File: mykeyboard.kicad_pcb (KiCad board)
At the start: 2 copper layers, 91.4 x 55.9 mm, 29 parts, among them J1 MJ-4PP-9, J2 LED, SW1 SW_PUSH, SW2 SW_PUSH, SW3 SW_PUSH, SW4 SW_PUSH, SW5 SW_PUSH, SW6 SW_PUSH, SW7 SW_PUSH, SW8 SW_PUSH, SW9 SW_PUSH, U1 ProMicro

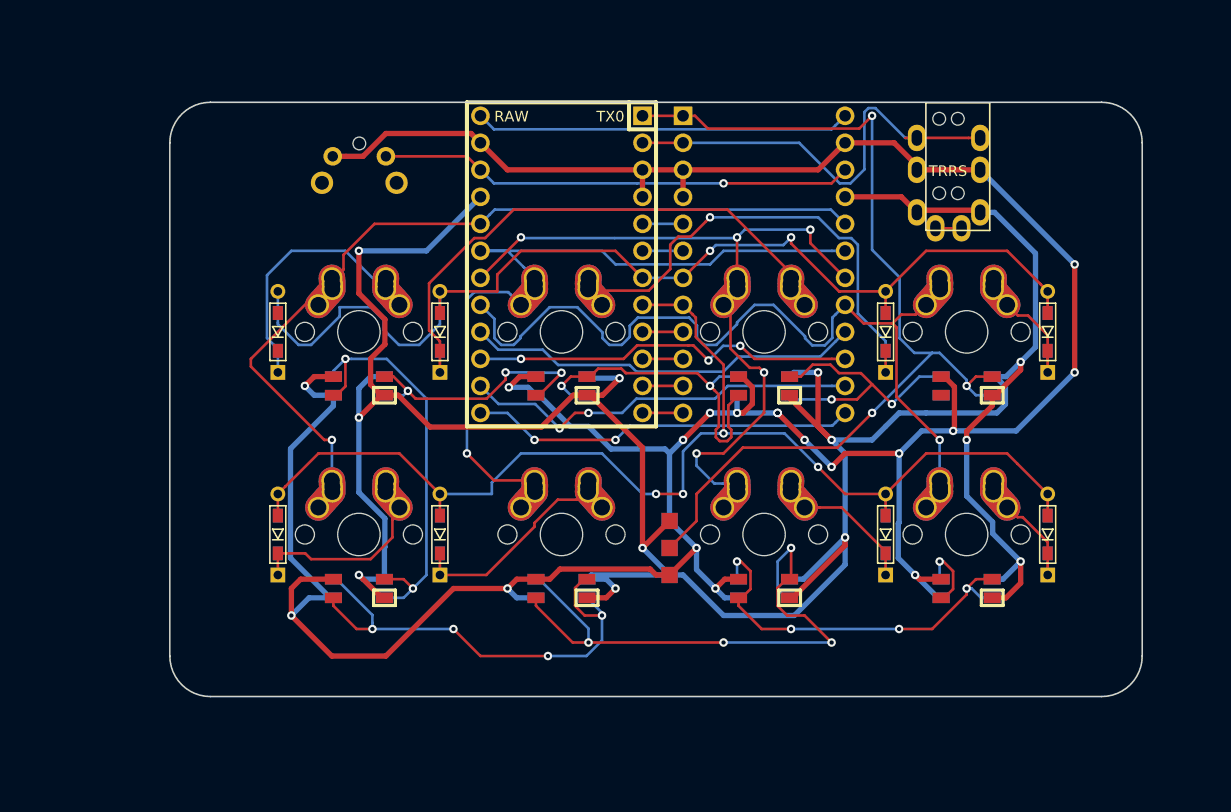
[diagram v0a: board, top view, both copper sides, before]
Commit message: スペーサの穴を確保
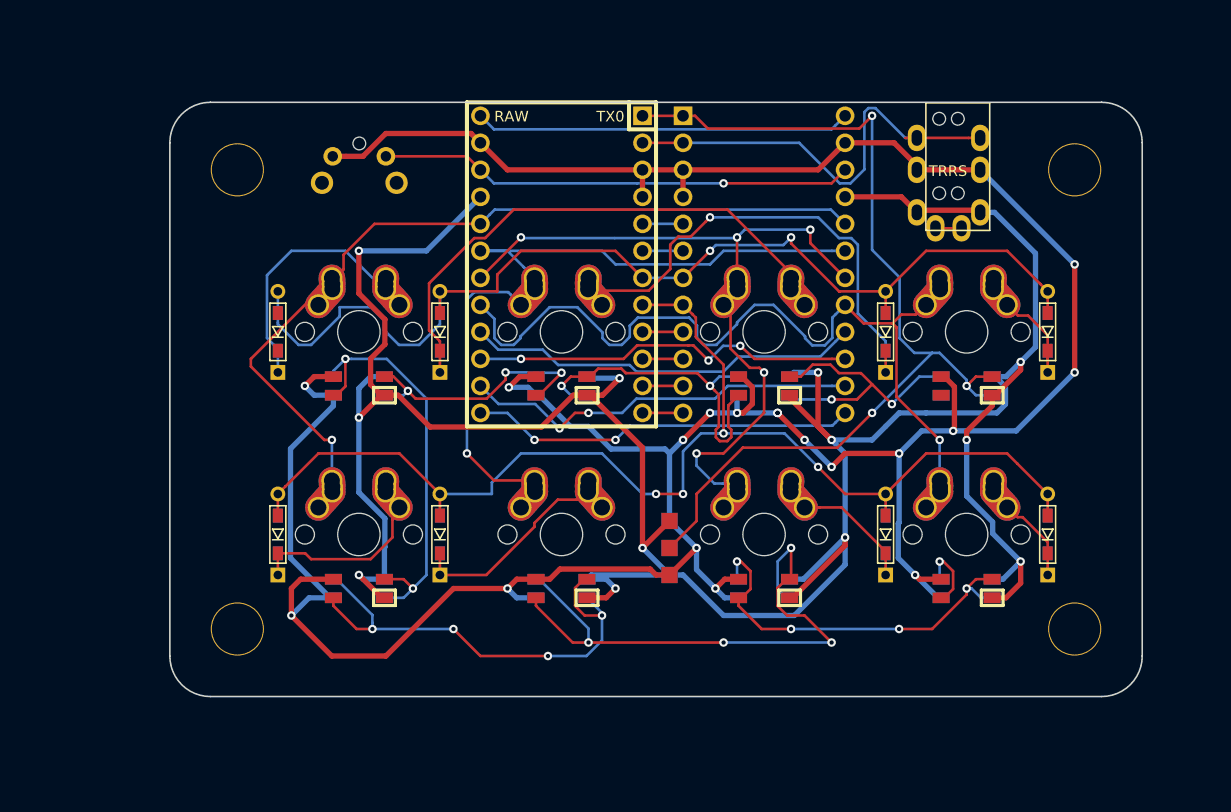
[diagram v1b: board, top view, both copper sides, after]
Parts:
- added Ref**: Val**, kbd:HOLE, F.Cu at (185.4, 81.3)
- added Ref**: Val**, kbd:HOLE, F.Cu at (185.4, 124.5)
- added Ref**: Val**, kbd:HOLE, F.Cu at (106.7, 124.5)
- added Ref**: Val**, kbd:HOLE, F.Cu at (106.7, 81.3)
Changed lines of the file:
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@@
     (tracks 725)
     (zones 0)
-    (modules 29)
+    (modules 33)
     (nets 40)
   )
@@
     (add_net row1)
   )
+  (module kbd:HOLE (layer F.Cu)
+    (at 185.42 81.28)
+    (descr "Mounting Hole 2.2mm, no annular, M2")
+    (tags "mounting hole 2.2mm no annular m2")
+    (attr virtual)
+    (fp_text reference Ref** (at 0 -3.2) (layer F.Fab)
+      (effects (font (size 1 1) (thickness 0.15)))
+    )
+    (fp_text value Val** (at 0 3.2) (layer F.Fab)
+      (effects (font (size 1 1) (thickness 0.15)))
+    )
+    (fp_text user %R (at 0.3 0) (layer F.Fab)
+      (effects (font (size 1 1) (thickness 0.15)))
+    )
+    (fp_circle (center 0 0) (end 2.2 0) (layer Cmts.User) (width 0.15))
+    (fp_circle (center 0 0) (end 2.45 0) (layer F.CrtYd) (width 0.05))
+    (pad "" np_thru_hole circle (at 0 0) (size 5 5) (drill 4.8) (layers *.Cu *.Mask))
+  )
+  (module kbd:HOLE (layer F.Cu)
+    (at 185.42 124.46)
+    (descr "Mounting Hole 2.2mm, no annular, M2")
+    (tags "mounting hole 2.2mm no annular m2")
+    (attr virtual)
+    (fp_text reference Ref** (at 0 -3.2) (layer F.Fab)
+      (effects (font (size 1 1) (thickness 0.15)))
+    )
+    (fp_text value Val** (at 0 3.2) (layer F.Fab)
+      (effects (font (size 1 1) (thickness 0.15)))
+    )
+    (fp_circle (center 0 0) (end 2.45 0) (layer F.CrtYd) (width 0.05))
+    (fp_circle (center 0 0) (end 2.2 0) (layer Cmts.User) (width 0.15))
+    (fp_text user %R (at 0.3 0) (layer F.Fab)
+      (effects (font (size 1 1) (thickness 0.15)))
+    )
+    (pad "" np_thru_hole circle (at 0 0) (size 5 5) (drill 4.8) (layers *.Cu *.Mask))
+  )
+  (module kbd:HOLE (layer F.Cu)
+    (at 106.68 124.46)
+    (descr "Mounting Hole 2.2mm, no annular, M2")
+    (tags "mounting hole 2.2mm no annular m2")
+    (attr virtual)
+    (fp_text reference Ref** (at 0 -3.2) (layer F.Fab)
+      (effects (font (size 1 1) (thickness 0.15)))
+    )
+    (fp_text value Val** (at 0 3.2) (layer F.Fab)
+      (effects (font (size 1 1) (thickness 0.15)))
+    )
+    (fp_text user %R (at 0.3 0) (layer F.Fab)
+      (effects (font (size 1 1) (thickness 0.15)))
+    )
+    (fp_circle (center 0 0) (end 2.2 0) (layer Cmts.User) (width 0.15))
+    (fp_circle (center 0 0) (end 2.45 0) (layer F.CrtYd) (width 0.05))
+    (pad "" np_thru_hole circle (at 0 0) (size 5 5) (drill 4.8) (layers *.Cu *.Mask))
+  )
+  (module kbd:HOLE (layer F.Cu)
+    (at 106.68 81.28)
+    (descr "Mounting Hole 2.2mm, no annular, M2")
+    (tags "mounting hole 2.2mm no annular m2")
+    (attr virtual)
+    (fp_text reference Ref** (at 0 -3.2) (layer F.Fab)
+      (effects (font (size 1 1) (thickness 0.15)))
+    )
+    (fp_text value Val** (at 0 3.2) (layer F.Fab)
+      (effects (font (size 1 1) (thickness 0.15)))
+    )
+    (fp_circle (center 0 0) (end 2.45 0) (layer F.CrtYd) (width 0.05))
+    (fp_circle (center 0 0) (end 2.2 0) (layer Cmts.User) (width 0.15))
+    (fp_text user %R (at 0.3 0) (layer F.Fab)
+      (effects (font (size 1 1) (thickness 0.15)))
+    )
+    (pad "" np_thru_hole circle (at 0 0) (size 5 5) (drill 4.8) (layers *.Cu *.Mask))
+  )
   (module Keebio-Parts:Hybrid_PCB_100H_Dual_hole (layer F.Cu)

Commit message: GND の塗りつぶし
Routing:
- added copper zone on B.Cu, net GND
- added copper zone on F.Cu, net GND
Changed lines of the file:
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@@
   (segment (start 172.72 119.635) (end 172.86 119.775) (width 0.25) (layer B.Cu) (net 39))
   (segment (start 172.72 118.11) (end 172.72 119.635) (width 0.25) (layer B.Cu) (net 39))
+  (zone (net 14) (net_name GND) (layer F.Cu) (hatch edge 0.508)
+    (connect_pads (clearance 0.508))
+    (min_thickness 0.254)
+    (fill yes (arc_segments 16) (thermal_gap 0.508) (thermal_bridge_width 0.508))
+    (polygon
+      (pts
+        (xy 194.31 133.35) (xy 194.31 73.66) (xy 99.06 72.39) (xy 96.52 130.81) (xy 99.06 135.89)
+      )
+    )
+  )
+  (zone (net 14) (net_name GND) (layer B.Cu) (hatch edge 0.508)
+    (connect_pads (clearance 0.508))
+    (min_thickness 0.254)
+    (fill yes (arc_segments 16) (thermal_gap 0.508) (thermal_bridge_width 0.508))
+    (polygon
+      (pts
+        (xy 196.85 134.62) (xy 198.12 72.39) (xy 86.36 67.31) (xy 90.17 139.7)
+      )
+    )
+  )
 )

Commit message: Add credit
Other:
- board text added: "wktk/id1kb v0.1 (2019-01-30) Designed by @wk wktk.jp/"
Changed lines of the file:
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@@
   (general
     (thickness 1.6)
-    (drawings 8)
+    (drawings 10)
     (tracks 725)
     (zones 0)
@@
     )
   )
+  (gr_text "wktk/id1kb v0.1 (2019-01-30)\nDesigned by @wk wktk.jp/" (at 187.96 88.9 90) (layer B.SilkS)
+    (effects (font (size 1.2 1.2) (thickness 0.2)) (justify left mirror))
+  )
+  (gr_text "wktk/id1kb v0.1 (2019-01-30)\nDesigned by @wk wktk.jp/" (at 187.96 116.84 90) (layer F.SilkS)
+    (effects (font (size 1.2 1.2) (thickness 0.2)) (justify left))
+  )
   (gr_line (start 100.33 78.74) (end 100.33 127) (layer Edge.Cuts) (width 0.15))

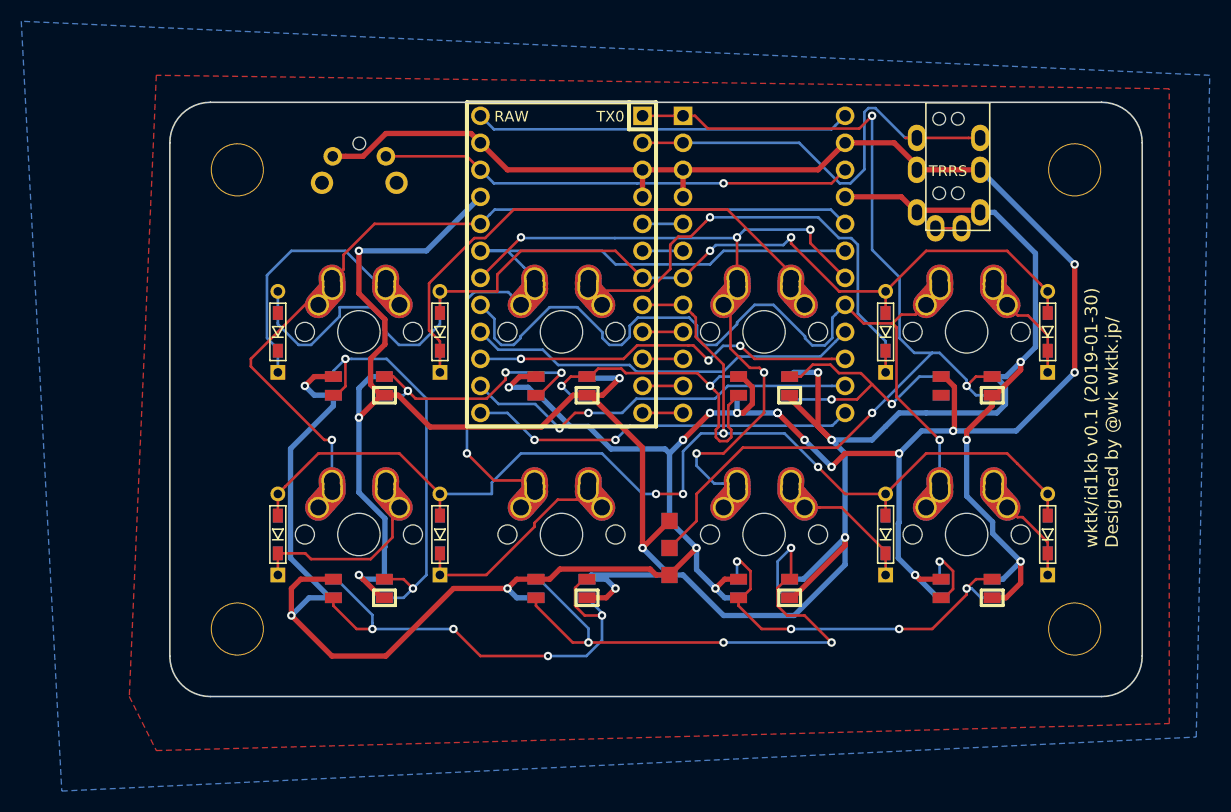
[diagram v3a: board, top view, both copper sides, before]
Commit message: 余裕がありそうなのでクレカサイズに変更、配線位置を一部内側に
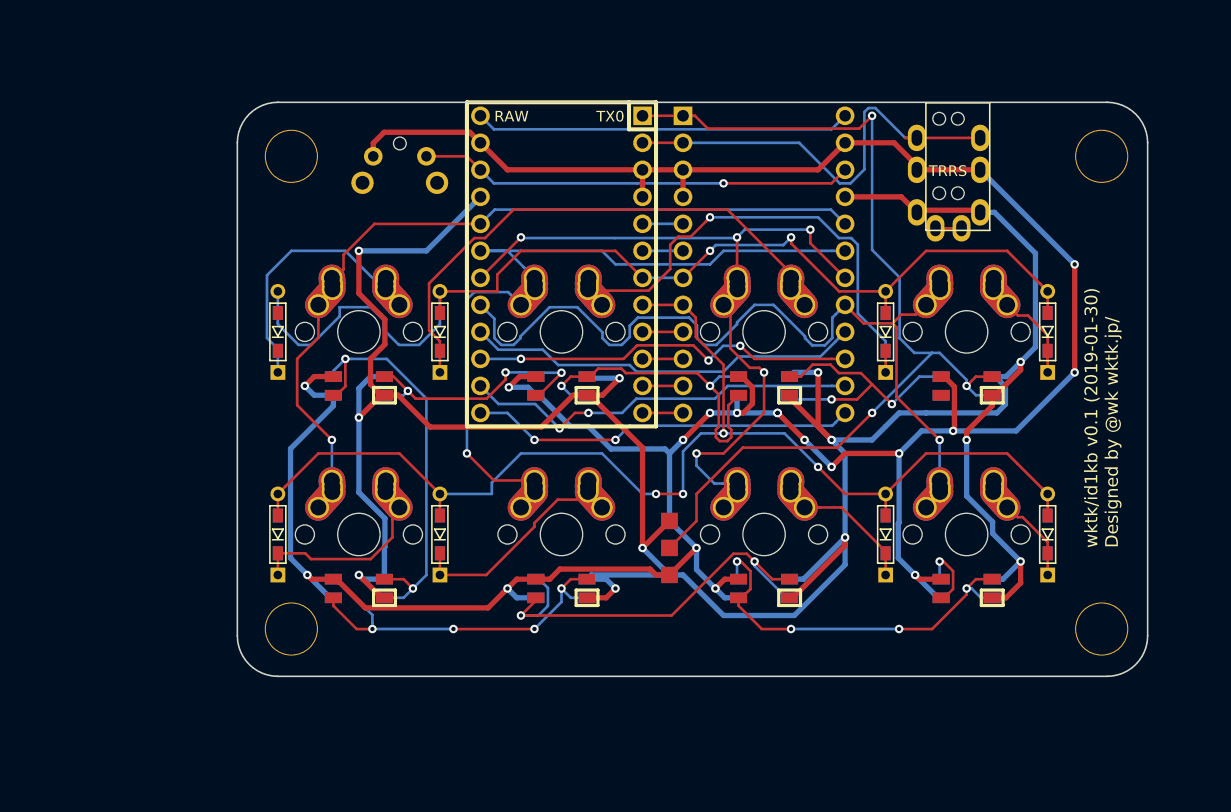
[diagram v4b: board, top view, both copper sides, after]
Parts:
- moved Ref** 5.24 mm to (111.8, 80.0)
- moved Ref** 5.08 mm to (111.8, 124.5)
- moved SW9 3.81 mm to (124.5, 80.0)
- moved Ref** 2.84 mm to (188.0, 80.0)
- moved Ref** 2.54 mm to (188.0, 124.5)
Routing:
- net GND: track 297.2 -> 279.6 mm
- net Net-(L4-Pad1): track 56.7 -> 41.9 mm, vias 4 -> 2
- net Net-(L2-Pad1): track 45.6 -> 37.3 mm
- net col0: track 79.3 -> 72.2 mm
- net reset: track 44.8 -> 40.9 mm
- removed copper zone on B.Cu, net GND
- removed copper zone on F.Cu, net GND
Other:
- board size 91.4 x 55.9 mm -> 85.6 x 54 mm

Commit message: GND を塗りつぶし
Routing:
- added copper zone on B.Cu, net GND
- added copper zone on F.Cu, net GND
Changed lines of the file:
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@@
   (segment (start 172.72 119.635) (end 172.86 119.775) (width 0.25) (layer B.Cu) (net 39))
   (segment (start 172.72 118.11) (end 172.72 119.635) (width 0.25) (layer B.Cu) (net 39))
+  (zone (net 14) (net_name GND) (layer F.Cu) (hatch edge 0.508)
+    (connect_pads (clearance 0.508))
+    (min_thickness 0.254)
+    (fill yes (arc_segments 16) (thermal_gap 0.508) (thermal_bridge_width 0.508))
+    (polygon
+      (pts
+        (xy 105.41 71.12) (xy 194.31 71.12) (xy 194.31 130.81) (xy 105.41 130.81)
+      )
+    )
+  )
+  (zone (net 14) (net_name GND) (layer B.Cu) (hatch edge 0.508)
+    (connect_pads (clearance 0.508))
+    (min_thickness 0.254)
+    (fill yes (arc_segments 16) (thermal_gap 0.508) (thermal_bridge_width 0.508))
+    (polygon
+      (pts
+        (xy 194.31 71.12) (xy 194.31 130.81) (xy 105.41 130.81) (xy 105.41 71.12)
+      )
+    )
+  )
 )
